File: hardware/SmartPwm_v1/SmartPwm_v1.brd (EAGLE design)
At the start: 101.6 x 83.8 mm, 41 parts, among them IC1 7805T, J1 ESP32-PICO-KIT, Q1 IRF3704-H, Q2 IRF3704-H, Q3 IRF3704-H, Q4 IRF3704-H, U1 ICL7667CBAZA, U3 ICL7667CBAZA

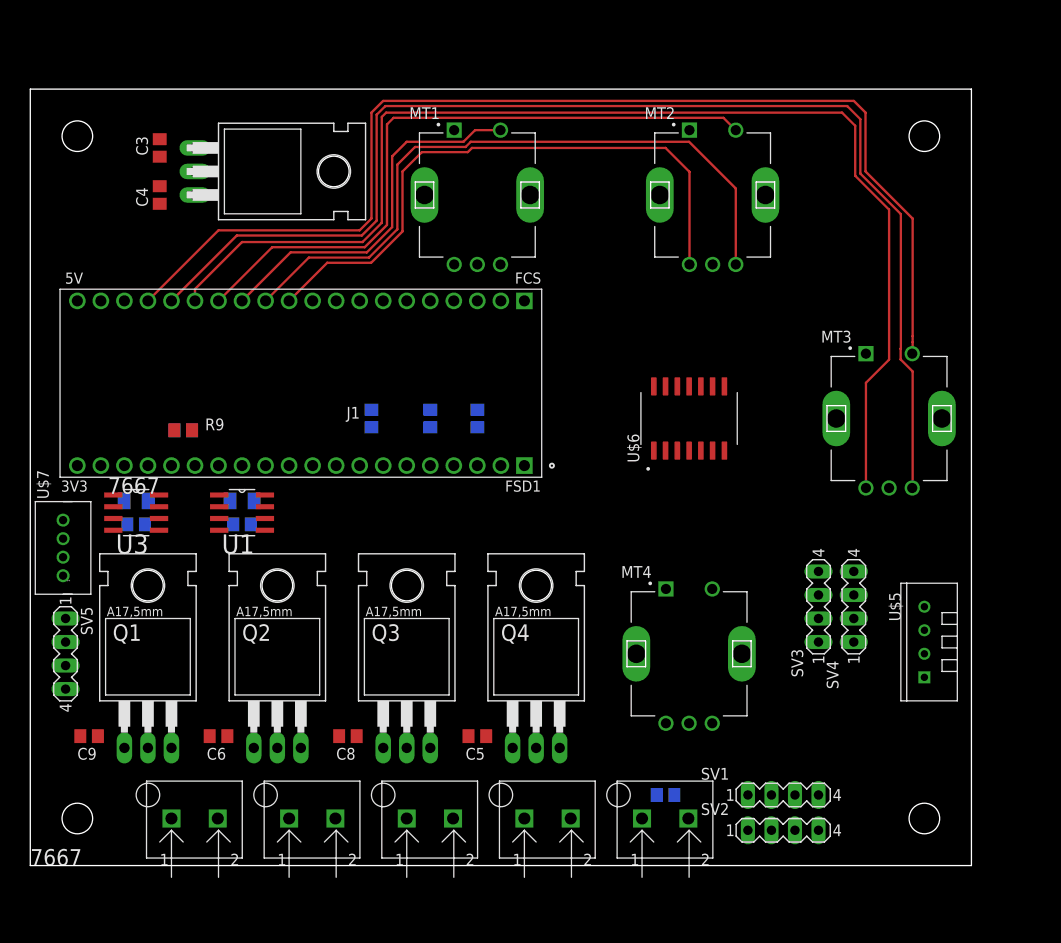
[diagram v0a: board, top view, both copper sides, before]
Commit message: did routing, but need to fix ctrl pins, since they were routed to inputs on the pico kit...
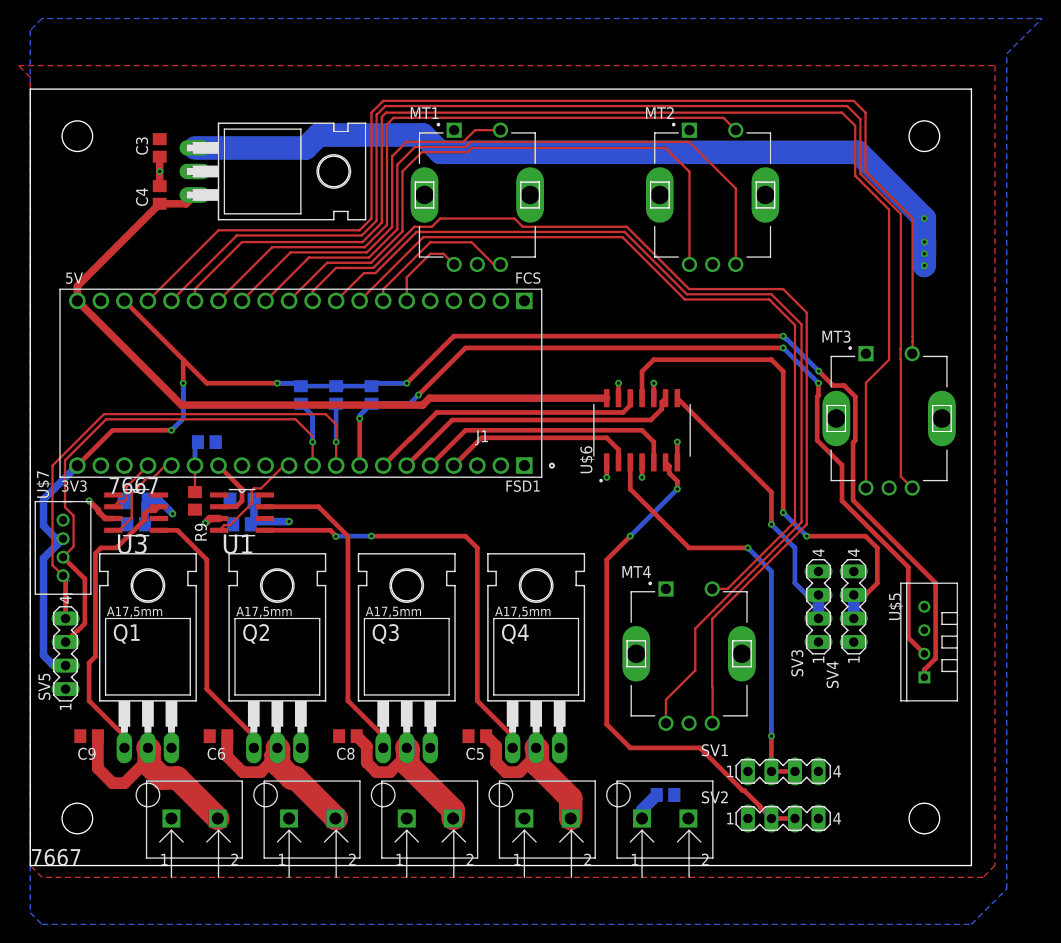
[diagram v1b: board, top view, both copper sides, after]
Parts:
- moved R8 19.2 mm to (29.2, 50.8)
- moved R7 10.5 mm to (33.0, 50.8)
- moved R9 7.73 mm to (17.8, 39.4), turned to 90 degrees
- moved U$6 5.24 mm to (66.0, 47.0)
- moved R10 2.84 mm to (19.1, 45.7)
- moved SV1 2.54 mm to (81.3, 10.2)
- moved R6 2.54 mm to (36.8, 50.8)
- moved SV2 1.27 mm to (81.3, 5.08)
- turned SV5 to 90 degrees
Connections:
- net CTRL4: now also J1.J2_11; no longer J1.J2_15
- net GND: now also U$6.10
- net K1A: now also J1.J3_6
- net K1B: now also J1.J3_7
- net K4A: now also J1.J3_9
- net K4B: now also J1.J3_10
- net K4S: now also J1.J3_8
- net LDAT1_3V3: now also J1.J2_4; no longer J1.J2_11
- net LDAT2_3V3: now also J1.J2_5; no longer J1.J2_10
- net LDAT3_3V3: now also J1.J2_6; no longer J1.J2_9
- net LDAT4_3V3: now also J1.J2_7; no longer J1.J2_8
- net SCL: now also J1.J2_9
- net SDA: now also J1.J2_10
- net TDAT: now also J1.J2_8
- net VCC: no longer U$6.10
- net VDIV: now also J1.J2_15
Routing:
- net VEE: track 0.00 -> 169.2 mm, vias 0 -> 6
- net K4B: track 0.00 -> 110.4 mm
- net K4A: track 0.00 -> 106.6 mm
- net VDD: track 0.00 -> 105.4 mm, vias 0 -> 6
- net TDAT: track 0.00 -> 93.6 mm, vias 0 -> 4
- net K4S: track 0.00 -> 86.9 mm
- net VCC: track 0.00 -> 80.5 mm
- net SDA: track 0.00 -> 59.5 mm, vias 0 -> 1
- net SCL: track 0.00 -> 59.0 mm, vias 0 -> 1
- net LDAT2_5V: track 0.00 -> 56.5 mm, vias 0 -> 2
- net LDAT4_5V: track 0.00 -> 55.6 mm, vias 0 -> 2
- net GATE4: track 0.00 -> 47.0 mm, vias 0 -> 2
- net LDAT1_5V: track 0.00 -> 45.9 mm, vias 0 -> 2
- net GATE3: track 0.00 -> 34.7 mm
- net GATE1: track 0.00 -> 32.2 mm
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- added copper zone on layer 16, net GND
- added copper zone on layer 1, net VDD

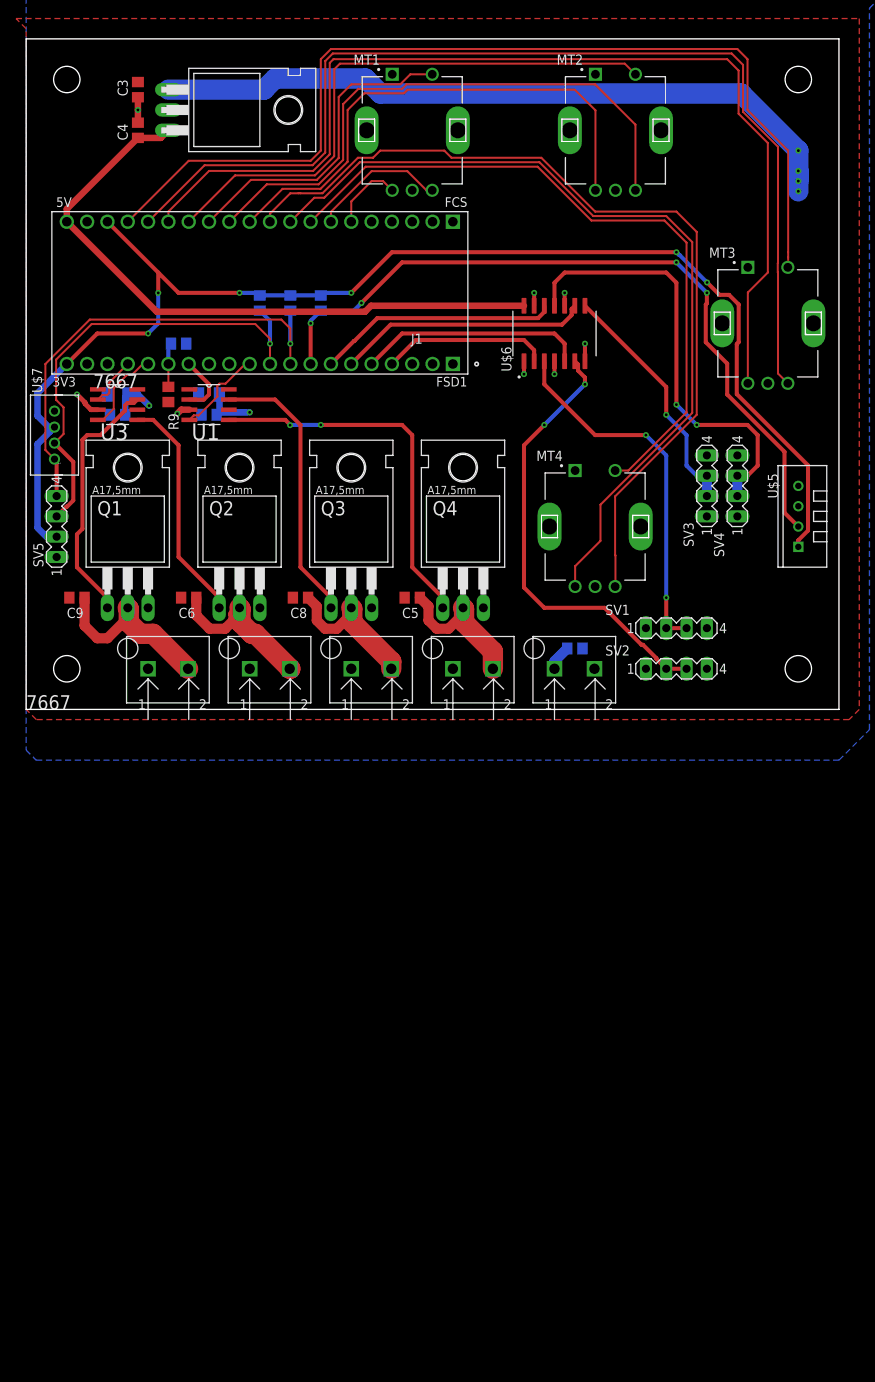
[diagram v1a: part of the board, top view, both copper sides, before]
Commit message: begin schematic for nano BLE sense based pwm module
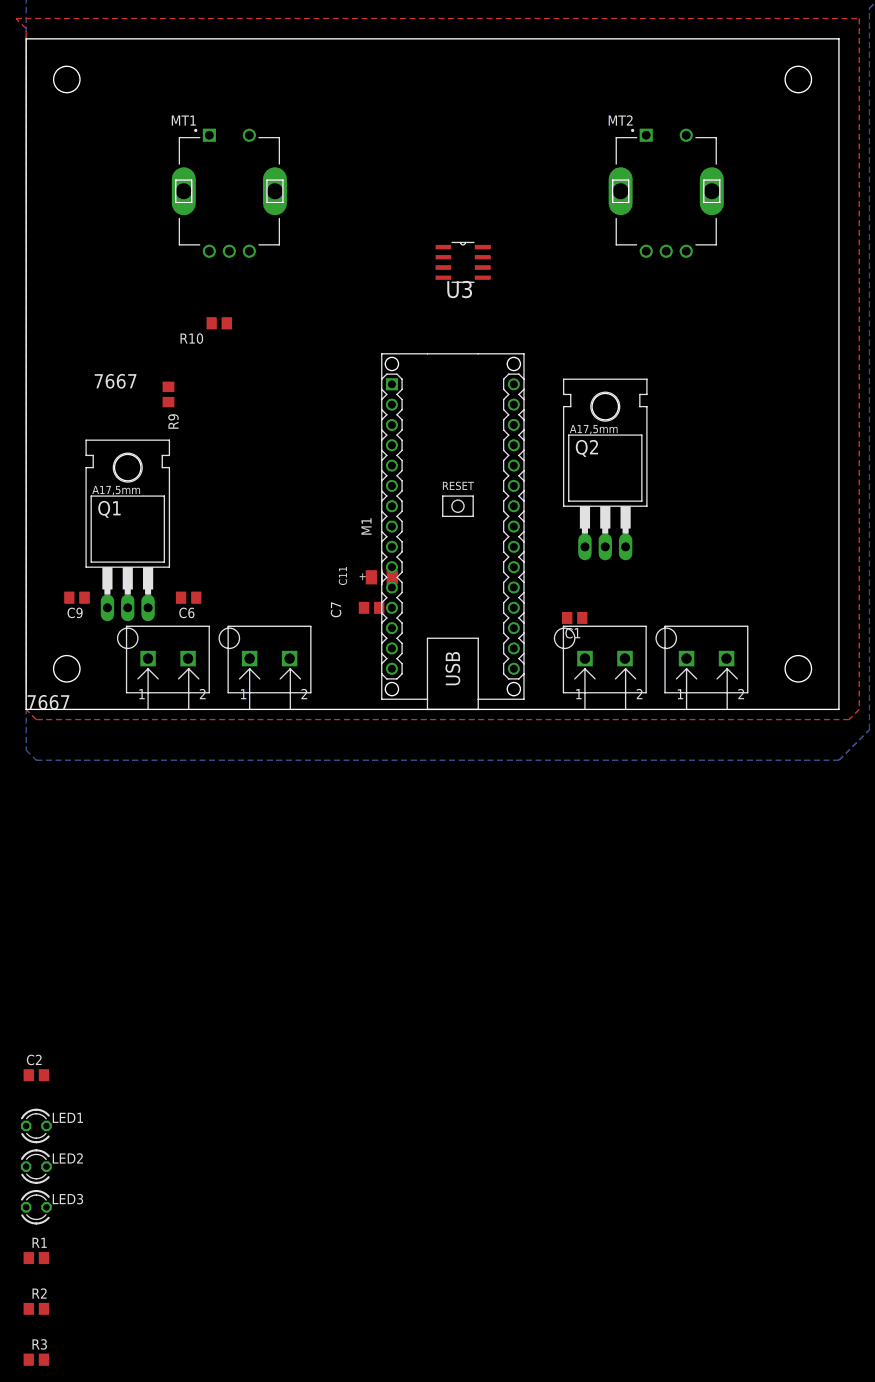
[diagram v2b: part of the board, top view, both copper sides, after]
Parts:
- removed C10: AVX_TPSA475K020R1800AVX_TPSA475K020R1800_0_0, AVX - TPSA475K020R1800:AVX_TPSA475K020R1800_0
- removed C12, C4: .1uf, rcl:C0805
- removed C3: .33uf, rcl:C0805
- removed C5, C8: 10uf, rcl:C0805
- removed IC1: 7805T, linear:TO220H
- removed J1: ESP32-PICO-KIT, ESP32-PICO-KIT:XCVR_ESP32-PICO-KIT
- removed MT3, MT4: PEC11R-4215F-S0024, PEC11R-4215F-S0024:XDCR_PEC11R-4215F-S0024
- removed Q3, Q4: IRF3704-H, transistor-power:TO220BH
- removed R6, R8: 10K, rcl:R0805
- removed R7: 10k, rcl:R0805
- removed SV1, SV2, SV3, SV4, SV5: (no value), con-lstb:MA04-1
- removed U$3, U$4: TB002-500-P02, mylib:TB002-500-P02
- removed U$6: 74AHTC125NSR, DIP794W45P254L1969H508Q14:SOP127P780X200-14N
- removed U$7: 110990030, seeedgrove:110990030-VERTICAL-GROVE-CONNECTOR
- removed U1: ICL7667CBAZA, ICL7667CBAZA:SOIC127P600X175-8N
- added C2: 10uf, rcl:C0805
- added LED1, LED2, LED3: TLLR4400, led:LED3MM
- added M1: ARDUINO-NANO-3.0, diy-modules:ARDUINO-NANO-3.0
- added R1, R2, R3: 220, rcl:R0805
- U$5: value TEMP-HUM-SENSOR-DHT11 -> TB002-500-P02; device diy-modules:TEMP-HUM-SENSOR-DHT11 -> mylib:TB002-500-P02
- moved U3 46.7 mm to (54.6, 55.9)
- moved Q2 46.4 mm to (72.4, 26.7)
- moved C11 40.2 mm to (44.5, 16.5), flipped to the top
- moved C7 39.9 mm to (43.2, 12.7), flipped to the top
- moved U$5 32.1 mm to (69.8, 6.35), turned to 0 degrees
- moved MT1 24.1 mm to (25.4, 64.8)
- moved U$8 16.6 mm to (82.5, 6.35)
- moved MT2 9.92 mm to (80.0, 64.8)
- moved R10 5.68 mm to (24.1, 48.3), flipped to the top
- moved C1 3.81 mm to (68.6, 11.4), flipped to the top, turned to 0 degrees
- moved U$1 1.27 mm to (15.2, 6.35)
- moved U$2 1.27 mm to (27.9, 6.35)
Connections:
- removed net GATE3: Q3.G, U1.7
- removed net GATE4: Q4.G, U1.5
- removed net K3A: J1.J3_15, MT3.A
- removed net K3B: J1.J3_16, MT3.B
- removed net K3S: J1.J3_17, MT3.2
- removed net K4A: J1.J3_9, MT4.A
- removed net K4B: J1.J3_10, MT4.B
- removed net K4S: J1.J3_8, MT4.2
- removed net LDAT1_3V3: J1.J2_4, U$6.2
- removed net LDAT1_5V: SV1.2, SV1.3, U$6.3
- removed net LDAT2_3V3: J1.J2_5, U$6.5
- removed net LDAT2_5V: SV2.2, SV2.3, U$6.6
- removed net LDAT3_3V3: J1.J2_6, U$6.9
- removed net LDAT3_5V: SV3.2, SV3.3, U$6.8
- removed net LDAT4_3V3: J1.J2_7, U$6.12
- removed net LDAT4_5V: SV4.2, SV4.3, U$6.11
- removed net LOAD_RET3: C8.2, Q3.D, U$3.P$2
- removed net LOAD_RET4: C5.2, Q4.D, U$4.P$2
- removed net SCL: J1.J2_9, R7.2, SV5.4, U$7.1
- removed net SDA: J1.J2_10, R8.2, SV5.3, U$7.2
- removed net TDAT: J1.J2_8, R6.2, U$5.2
- new net D1_N: LED1.K, M1.J1.1
- new net D2_N: LED2.K, M1.J1.2
- new net D3_N: LED3.K, M1.J1.15
- new net N$1: LED1.A, R1.1
- new net N$2: LED2.A, R2.1
- new net N$3: LED3.A, R3.1
- net CTRL1: now also M1.J1.12; no longer J1.J2_17
- net CTRL2: now also M1.J1.13; no longer J1.J2_16
- net CTRL3: now also M1.J1.14; no longer J1.J2_14, U1.2
- net CTRL4: now also M1.J1.6; no longer J1.J2_11, U1.4
- net GND: now also C2.2, M1.J1.4, M1.J2.2, U$5.P$2; no longer C10.1, C12.2, C3.2, C4.2, IC1.2, J1.J2_19, J1.J3_19, MT3.1, MT3.COM, MT3.S1, MT3.S2, MT4.1, MT4.COM, MT4.S1, MT4.S2, Q3.S, Q4.S, SV1.1, SV2.1, SV3.1, SV4.1, SV5.1, U$5.4, U$6.1, U$6.10, U$6.13, U$6.4, U$6.7, U$7.4, U1.3
- net K1A: now also M1.J1.7; no longer J1.J3_6
- net K1B: now also M1.J1.8; no longer J1.J3_7
- net K1S: now also M1.J1.9; no longer J1.J3_13
- net K2A: now also M1.J1.10; no longer J1.J3_11
- net K2B: now also M1.J1.11; no longer J1.J3_12
- net K2S: now also M1.J1.5; no longer J1.J3_14
- net VCC: now also M1.J2.4; no longer C4.1, IC1.3, J1.J3_20, U$6.14
- net VDD: now also C2.1, M1.J2.1, U$5.P$1; no longer C10.2, C12.1, C3.1, C5.1, C8.1, IC1.1, SV1.4, SV2.4, SV3.4, SV4.4, U$3.P$1, U$4.P$1, U1.6
- net VDIV: now also M1.J2.12; no longer J1.J2_15
- net VEE: now also M1.J2.14, R1.2, R2.2, R3.2; no longer J1.J2_20, J1.J3_18, R6.1, R7.1, R8.1, SV5.2, U$5.1, U$7.3
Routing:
- net VEE: track 169.2 -> 0.00 mm, vias 6 -> 0
- net K3B: track 132.5 -> 0.00 mm
- net K3A: track 129.4 -> 0.00 mm
- net K3S: track 121.8 -> 0.00 mm
- net K4B: track 110.4 -> 0.00 mm
- net K4A: track 106.6 -> 0.00 mm
- net VDD: track 105.4 -> 0.00 mm, vias 6 -> 0
- net TDAT: track 93.6 -> 0.00 mm, vias 4 -> 0
- net K4S: track 86.9 -> 0.00 mm
- net VCC: track 80.5 -> 0.00 mm
- net K2B: track 72.2 -> 0.00 mm
- net K2S: track 70.9 -> 0.00 mm
- net K2A: track 64.9 -> 0.00 mm
- net SDA: track 59.5 -> 0.00 mm, vias 1 -> 0
- net SCL: track 59.0 -> 0.00 mm, vias 1 -> 0
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
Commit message: back to through hole design...
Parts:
- removed C11: AVX_TPSA475K020R1800AVX_TPSA475K020R1800_0_0, AVX - TPSA475K020R1800:AVX_TPSA475K020R1800_0
- removed C7: .1uf, rcl:C0805
- removed C9: 10uf, rcl:C0805
- removed R10: 5K, rcl:R0805
- removed R9: 25K, rcl:R0805
- added C3, C4: 10uF, rcl:C025-024X044
- added C5: .1uF, rcl:C025-024X044
- added R4: 25K, rcl:0207/10
- added R5: 5K, rcl:0207/10
- added U1: ICL7667CPAZ, ICL7667CPAZ:DIP254P762X533-8
- C1, C2: value 10uf -> 10uF; device rcl:C0805 -> rcl:C025-024X044
- C6: value 10uf -> 4.7uF; device rcl:C0805 -> rcl:C025-024X044
- R1, R2, R3: device rcl:R0805 -> rcl:0207/10
- moved C6 174.6 mm to (-12.7, -157.5)
- moved C1 160.5 mm to (-12.7, -127.0)
- moved C2 90.0 mm to (-12.7, -134.6)
- moved R1 37.0 mm to (-8.89, -104.1)
- moved R2 35.8 mm to (-8.89, -109.2)
- moved R3 34.5 mm to (-8.89, -114.3)
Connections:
- net CTRL1: now also U1.2
- net CTRL2: now also U1.4
- net GATE1: now also U1.7
- net GATE2: now also U1.5
- net GND: now also C3.2, C4.2, C5.2, C6.2, R5.2, U1.3; no longer C1.2, C11.1, C2.2, C7.2, R10.2
- net LOAD_RET1: now also C1.2; no longer C9.2
- net LOAD_RET2: now also C2.2; no longer C6.2
- net VDD: now also C3.1, C4.1, C5.1, R4.1, U1.6; no longer C11.2, C7.1, C9.1, R9.1
- net VDIV: now also R4.2, R5.1; no longer R10.1, R9.2
